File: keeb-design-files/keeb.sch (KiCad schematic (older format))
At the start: 0 parts

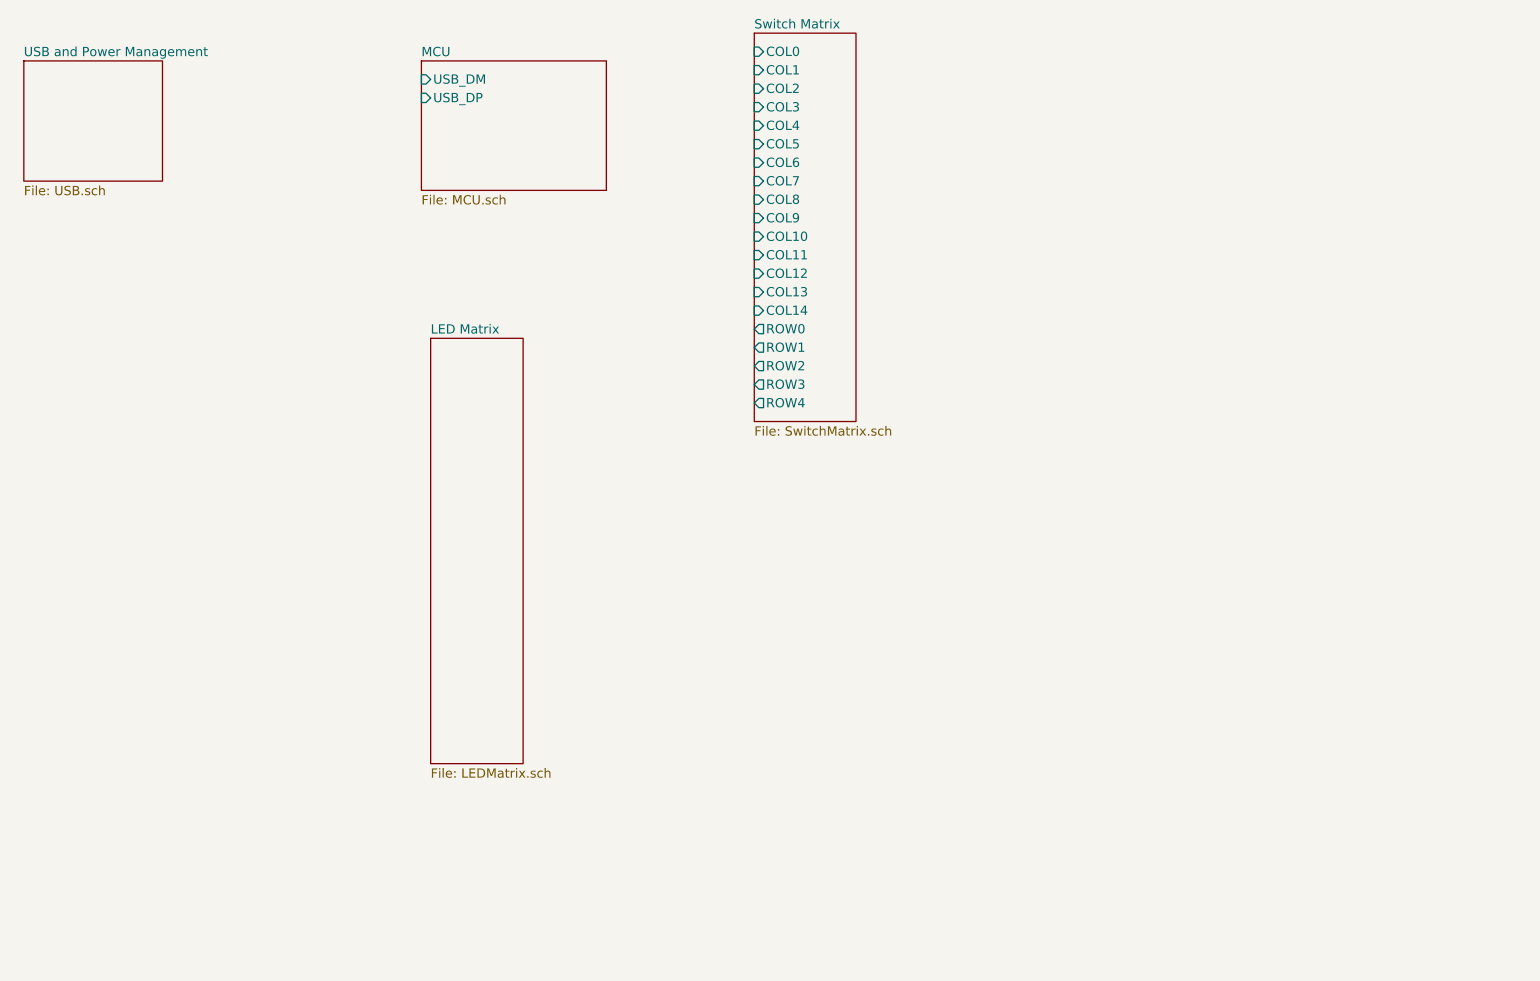
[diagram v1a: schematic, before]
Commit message: Add ESD diodes, USB isolator and LDO to schematic
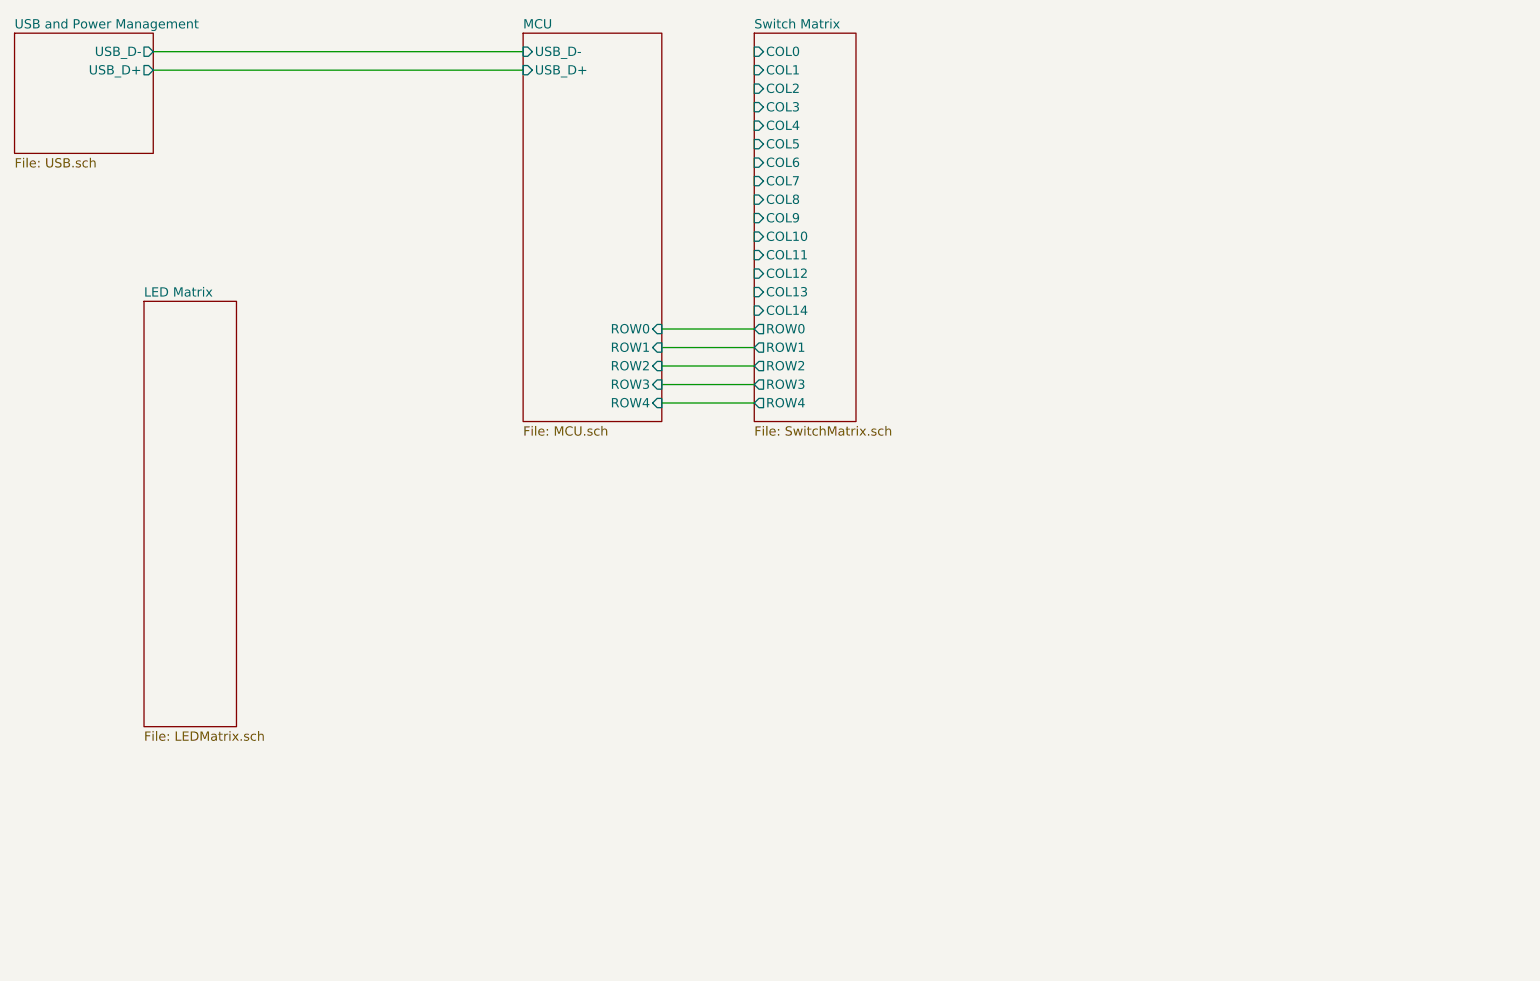
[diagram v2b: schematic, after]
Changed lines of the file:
@@
 $EndDescr
-$Sheet
-S 3250 1200 1000 700
-U 5EA13AF3
-F0 "MCU" 50
-F1 "MCU.sch" 50
-F2 "USB_DM" I L 3250 1300 50
-F3 "USB_DP" I L 3250 1400 50
-$EndSheet
 $Sheet
 S 5050 1050 550  2100
@@
 $EndSheet
 $Sheet
-S 1100 1200 750  650
+S 1050 1050 750  650
 U 5EFFF439
 F0 "USB and Power Management" 50
 F1 "USB.sch" 50
+F2 "USB_D-" O R 1800 1150 50
+F3 "USB_D+" O R 1800 1250 50
 $EndSheet
 $Sheet
-S 3300 2700 500  2300
+S 1750 2500 500  2300
 U 5F00D618
 F0 "LED Matrix" 50
 F1 "LEDMatrix.sch" 50
 $EndSheet
+$Sheet
+S 3800 1050 750  2100
+U 5EA13AF3
+F0 "MCU" 50
+F1 "MCU.sch" 50
+F2 "USB_D-" I L 3800 1150 50
+F3 "USB_D+" I L 3800 1250 50
+F4 "ROW0" I R 4550 2650 50
+F5 "ROW1" I R 4550 2750 50
+F6 "ROW2" I R 4550 2850 50
+F7 "ROW3" I R 4550 2950 50
+F8 "ROW4" I R 4550 3050 50
+$EndSheet
+Wire Wire Line
+	4550 2650 5050 2650
+Wire Wire Line
+	4550 2750 5050 2750
+Wire Wire Line
+	4550 2850 5050 2850
+Wire Wire Line
+	4550 2950 5050 2950
+Wire Wire Line
+	4550 3050 5050 3050
+Wire Wire Line
+	1800 1150 3800 1150
+Wire Wire Line
+	1800 1250 3800 1250
 $EndSCHEMATC

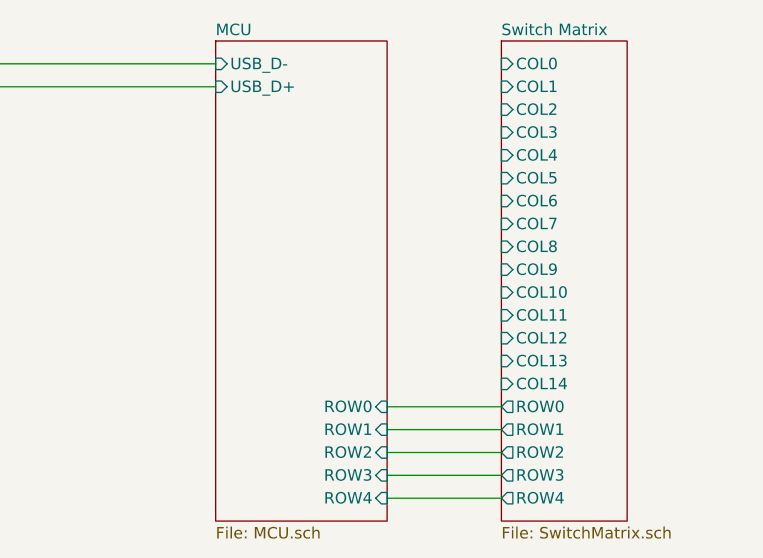
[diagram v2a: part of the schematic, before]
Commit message: Start Battery Management and routed matrix to STM32L0
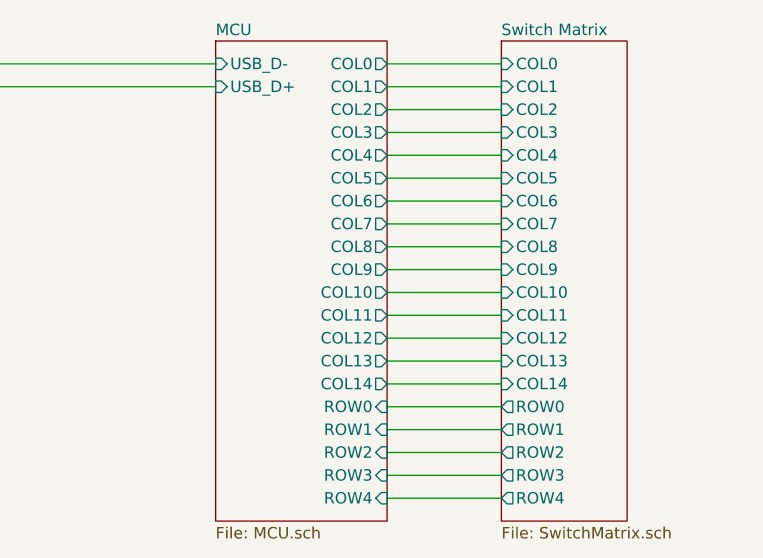
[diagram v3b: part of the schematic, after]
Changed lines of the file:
@@
 F1 "LEDMatrix.sch" 50
-$EndSheet
-$Sheet
-S 3800 1050 750  2100
-U 5EA13AF3
-F0 "MCU" 50
-F1 "MCU.sch" 50
-F2 "USB_D-" I L 3800 1150 50
-F3 "USB_D+" I L 3800 1250 50
-F4 "ROW0" I R 4550 2650 50
-F5 "ROW1" I R 4550 2750 50
-F6 "ROW2" I R 4550 2850 50
-F7 "ROW3" I R 4550 2950 50
-F8 "ROW4" I R 4550 3050 50
 $EndSheet
 Wire Wire Line
@@
 Wire Wire Line
 	1800 1250 3800 1250
+$Sheet
+S 3800 1050 750  2100
+U 5EA13AF3
+F0 "MCU" 50
+F1 "MCU.sch" 50
+F2 "USB_D-" I L 3800 1150 50
+F3 "USB_D+" I L 3800 1250 50
+F4 "ROW0" I R 4550 2650 50
+F5 "ROW1" I R 4550 2750 50
+F6 "ROW2" I R 4550 2850 50
+F7 "ROW3" I R 4550 2950 50
+F8 "ROW4" I R 4550 3050 50
+F9 "COL0" O R 4550 1150 50
+F10 "COL1" O R 4550 1250 50
+F11 "COL2" O R 4550 1350 50
+F12 "COL3" O R 4550 1450 50
+F13 "COL4" O R 4550 1550 50
+F14 "COL5" O R 4550 1650 50
+F15 "COL6" O R 4550 1750 50
+F16 "COL7" O R 4550 1850 50
+F17 "COL8" O R 4550 1950 50
+F18 "COL9" O R 4550 2050 50
+F19 "COL10" O R 4550 2150 50
+F20 "COL11" O R 4550 2250 50
+F21 "COL12" O R 4550 2350 50
+F22 "COL13" O R 4550 2450 50
+F23 "COL14" O R 4550 2550 50
+$EndSheet
+Wire Wire Line
+	4550 1150 5050 1150
+Wire Wire Line
+	4550 1250 5050 1250
+Wire Wire Line
+	4550 1350 5050 1350
+Wire Wire Line
+	4550 1450 5050 1450
+Wire Wire Line
+	4550 1550 5050 1550
+Wire Wire Line
+	4550 1650 5050 1650
+Wire Wire Line
+	4550 1750 5050 1750
+Wire Wire Line
+	4550 1850 5050 1850
+Wire Wire Line
+	4550 1950 5050 1950
+Wire Wire Line
+	4550 2050 5050 2050
+Wire Wire Line
+	4550 2150 5050 2150
+Wire Wire Line
+	4550 2250 5050 2250
+Wire Wire Line
+	4550 2350 5050 2350
+Wire Wire Line
+	4550 2450 5050 2450
+Wire Wire Line
+	4550 2550 5050 2550
 $EndSCHEMATC

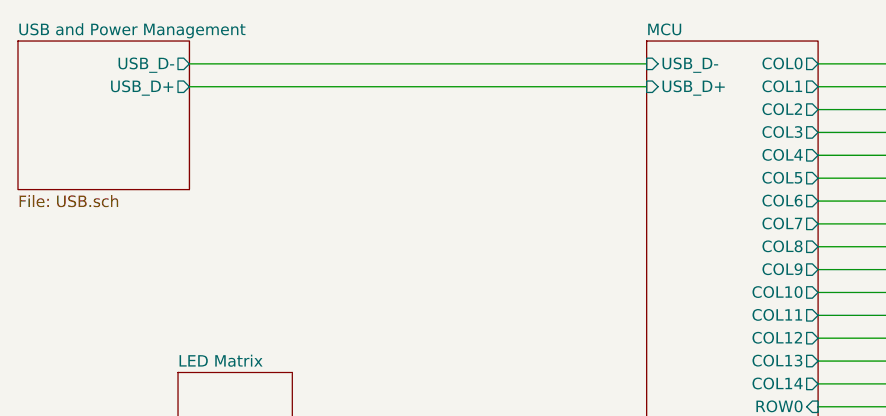
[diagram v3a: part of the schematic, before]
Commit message: Connect USB Hierarchical pins to MCU
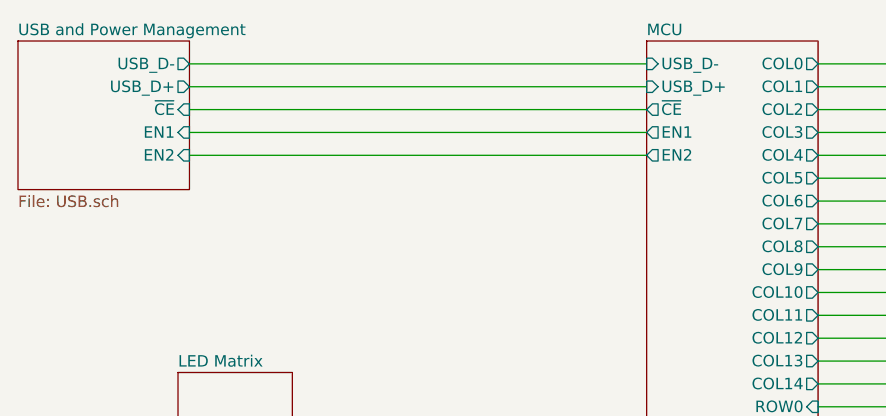
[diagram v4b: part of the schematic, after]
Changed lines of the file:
@@
 F2 "USB_D-" O R 1800 1150 50
 F3 "USB_D+" O R 1800 1250 50
+F4 "~CE~" I R 1800 1350 50
+F5 "EN1" I R 1800 1450 50
+F6 "EN2" I R 1800 1550 50
 $EndSheet
 $Sheet
@@
 F22 "COL13" O R 4550 2450 50
 F23 "COL14" O R 4550 2550 50
+F24 "~CE~" O L 3800 1350 50
+F25 "EN1" O L 3800 1450 50
+F26 "EN2" O L 3800 1550 50
 $EndSheet
 Wire Wire Line
@@
 Wire Wire Line
 	4550 2550 5050 2550
+Wire Wire Line
+	3800 1550 1800 1550
+Wire Wire Line
+	1800 1450 3800 1450
+Wire Wire Line
+	3800 1350 1800 1350
 $EndSCHEMATC

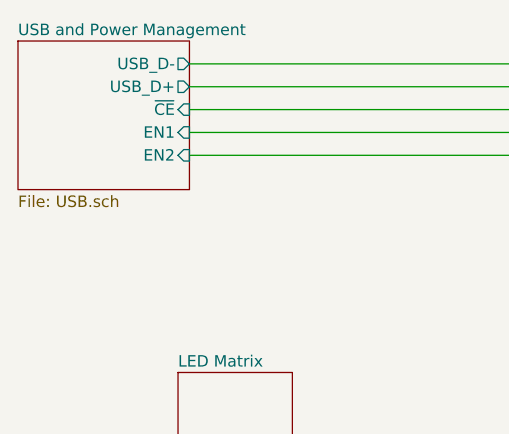
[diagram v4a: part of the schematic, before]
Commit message: Add I2C Pull-ups, Add STC3100 Fuel Guage
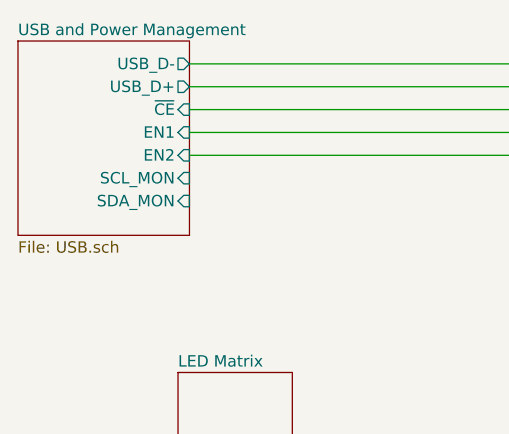
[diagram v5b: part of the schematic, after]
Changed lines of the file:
@@
 $EndSheet
 $Sheet
-S 1050 1050 750  650
+S 1050 1050 750  850
 U 5EFFF439
 F0 "USB and Power Management" 50
@@
 F5 "EN1" I R 1800 1450 50
 F6 "EN2" I R 1800 1550 50
+F7 "SCL_MON" I R 1800 1650 50
+F8 "SDA_MON" I R 1800 1750 50
 $EndSheet
 $Sheet

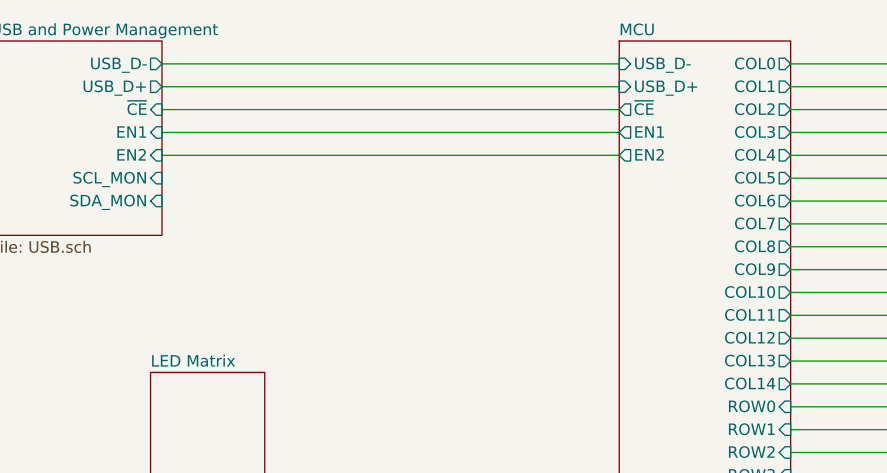
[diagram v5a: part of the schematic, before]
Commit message: Fix minor Batter Management issue
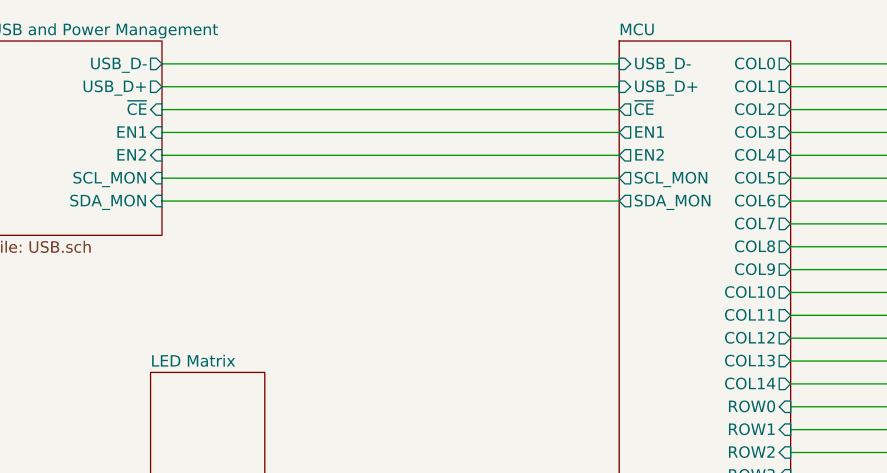
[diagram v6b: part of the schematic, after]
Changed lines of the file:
@@
 F25 "EN1" O L 3800 1450 50
 F26 "EN2" O L 3800 1550 50
+F27 "SCL_MON" O L 3800 1650 50
+F28 "SDA_MON" O L 3800 1750 50
 $EndSheet
 Wire Wire Line
@@
 Wire Wire Line
 	3800 1350 1800 1350
+Wire Wire Line
+	3800 1750 1800 1750
+Wire Wire Line
+	1800 1650 3800 1650
 $EndSCHEMATC

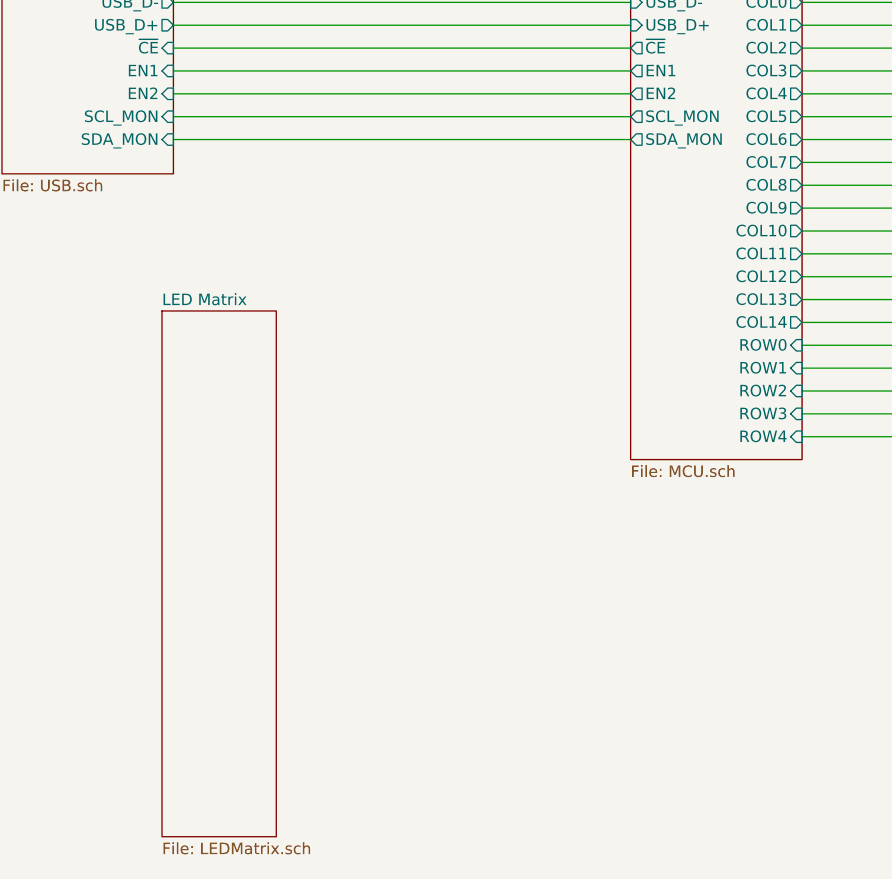
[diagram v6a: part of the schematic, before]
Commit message: Re-map MCU pins, Add LEDs, Remove USB Isolation cause it couldn't handle the POWER! More routing done
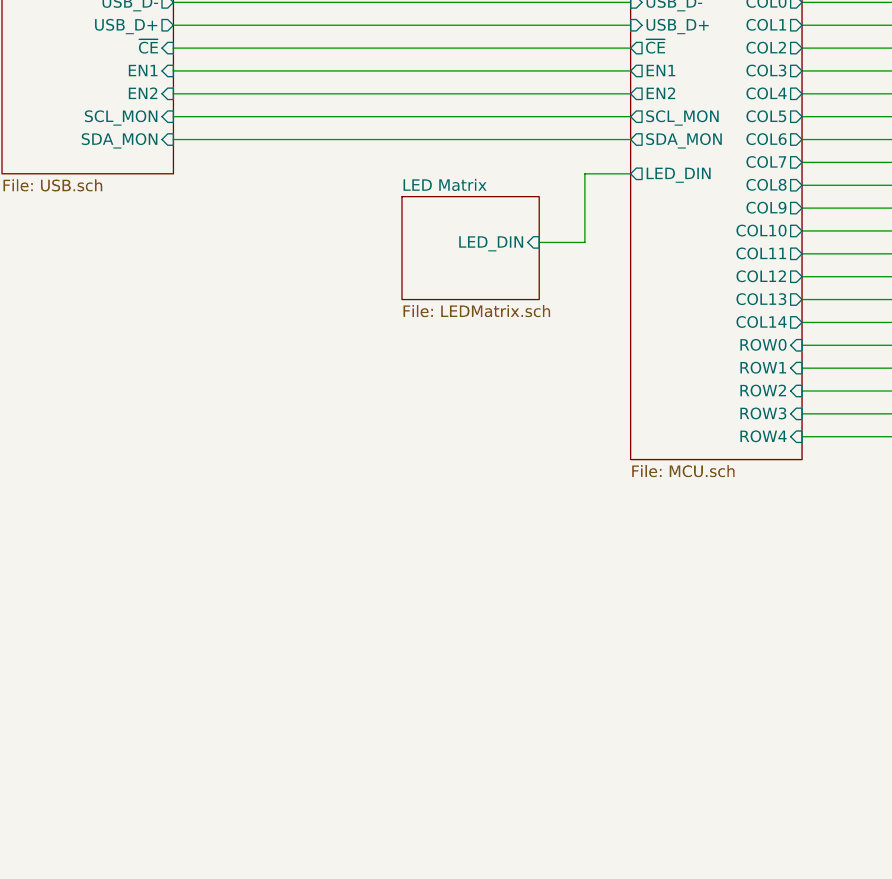
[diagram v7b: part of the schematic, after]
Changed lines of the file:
@@
 $EndSheet
 $Sheet
-S 1750 2500 500  2300
+S 2800 2000 600  450
 U 5F00D618
 F0 "LED Matrix" 50
 F1 "LEDMatrix.sch" 50
+F2 "LED_DIN" I R 3400 2200 50
 $EndSheet
 Wire Wire Line
@@
 F27 "SCL_MON" O L 3800 1650 50
 F28 "SDA_MON" O L 3800 1750 50
+F29 "LED_DIN" O L 3800 1900 50
 $EndSheet
 Wire Wire Line
@@
 Wire Wire Line
 	1800 1650 3800 1650
+Wire Wire Line
+	3400 2200 3600 2200
+Wire Wire Line
+	3600 2200 3600 1900
+Wire Wire Line
+	3600 1900 3800 1900
 $EndSCHEMATC

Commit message: Create gerbers picknplace and bom
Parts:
- added H1, H2, H3, H4: MountingHole, MountingHole:MountingHole_4.3mm_M4, symbol Mechanical:MountingHole
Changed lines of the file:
@@
 Wire Wire Line
 	3600 1900 3800 1900
+$Comp
+L Mechanical:MountingHole H4
+U 1 1 5ECAF7EB
+P 8500 6000
+F 0 "H4" H 8600 6046 50  0000 L CNN
+F 1 "MountingHole" H 8600 5955 50  0000 L CNN
+F 2 "MountingHole:MountingHole_4.3mm_M4" H 8500 6000 50  0001 C CNN
+F 3 "~" H 8500 6000 50  0001 C CNN
+	1    8500 6000
+	1    0    0    -1
+$EndComp
+$Comp
+L Mechanical:MountingHole H3
+U 1 1 5ECB0190
+P 8000 6000
+F 0 "H3" H 8100 6046 50  0000 L CNN
+F 1 "MountingHole" H 8100 5955 50  0000 L CNN
+F 2 "MountingHole:MountingHole_4.3mm_M4" H 8000 6000 50  0001 C CNN
+F 3 "~" H 8000 6000 50  0001 C CNN
+	1    8000 6000
+	1    0    0    -1
+$EndComp
+$Comp
+L Mechanical:MountingHole H2
+U 1 1 5ECB0231
+P 7500 6000
+F 0 "H2" H 7600 6046 50  0000 L CNN
+F 1 "MountingHole" H 7600 5955 50  0000 L CNN
+F 2 "MountingHole:MountingHole_4.3mm_M4" H 7500 6000 50  0001 C CNN
+F 3 "~" H 7500 6000 50  0001 C CNN
+	1    7500 6000
+	1    0    0    -1
+$EndComp
+$Comp
+L Mechanical:MountingHole H1
+U 1 1 5ECB02DE
+P 7000 6000
+F 0 "H1" H 7100 6046 50  0000 L CNN
+F 1 "MountingHole" H 7100 5955 50  0000 L CNN
+F 2 "MountingHole:MountingHole_4.3mm_M4" H 7000 6000 50  0001 C CNN
+F 3 "~" H 7000 6000 50  0001 C CNN
+	1    7000 6000
+	1    0    0    -1
+$EndComp
 $EndSCHEMATC
